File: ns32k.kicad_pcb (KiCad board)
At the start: 4 copper layers, 145.5 x 89.6 mm, 141 parts, among them J1 +5V SUPPLY, J2 3V3 Serial, J3 USB_C_USB2.0_16P, J4 RJ45, SW1 RESET, SW2 SW_DIP_x04, U1 NS32201, U10 74AHC373, U11 74AHC373, U12 74AHC138, U13 AS6C6416-55, U14 MT29F8G08ABACA, U15 MX29LV040C, U16 MX29LV040C, U17 ST16C550, U18 CP2102N, U19 74AHC32, U2 LM3671, U20 74AHC1GU04, U21 KSZ8851-16MLL, U22 74AHC245, U3 NS32016, U4 NS32082, U5 NS32202, U6 74AHC08, U7 74AHC245, U8 74AHC245, U9 74AHC373, Y1 12.00000MHz, Y2 7.3728MHz, Y3 25MHz

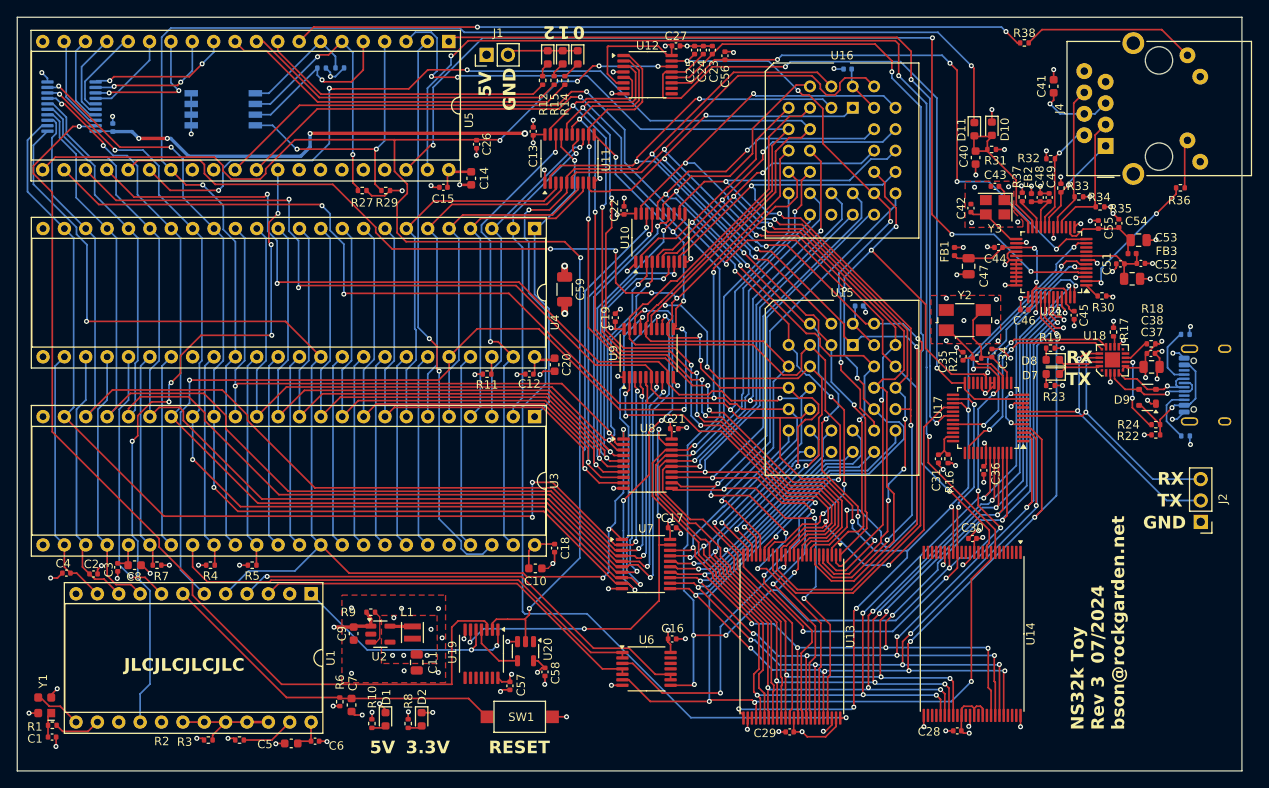
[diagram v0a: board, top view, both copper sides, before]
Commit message: Rework RESET/RST: see Changelist
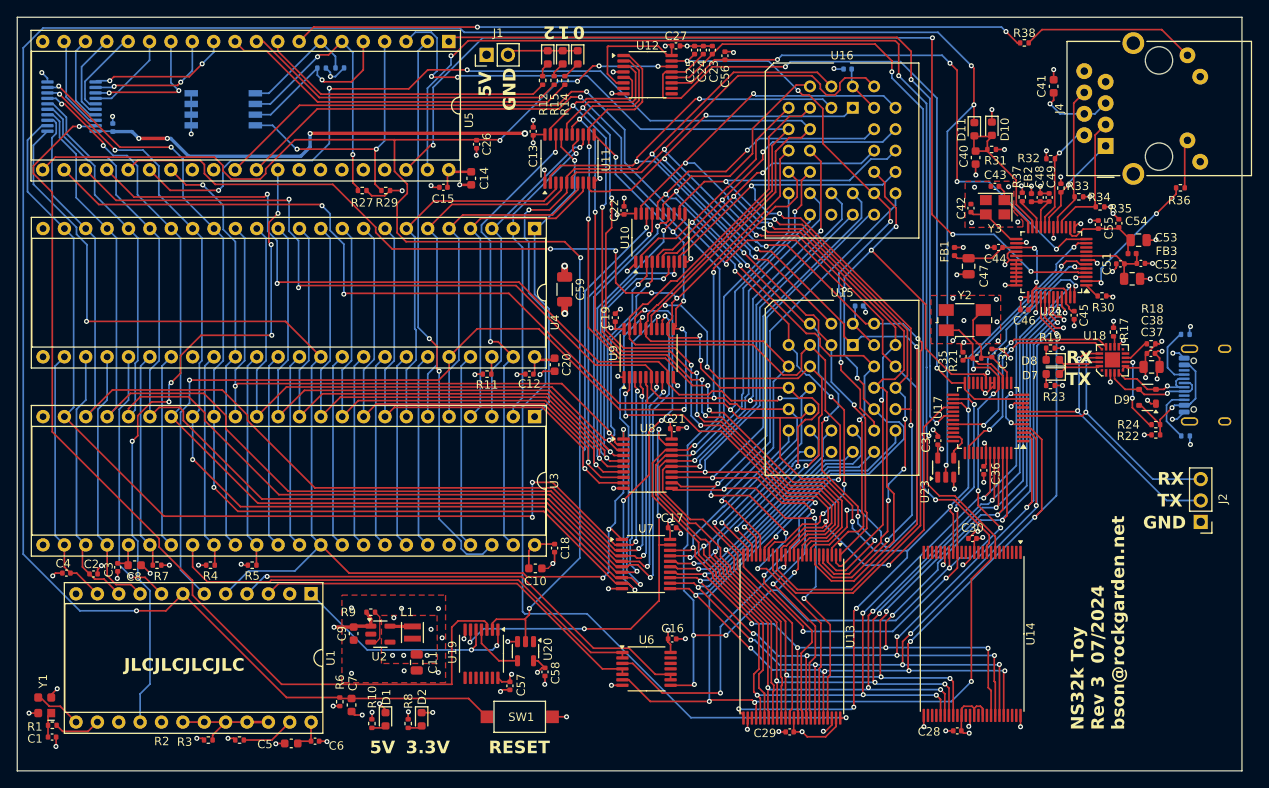
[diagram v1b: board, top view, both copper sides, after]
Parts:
- removed R16: 47k, Resistor_SMD:R_0402_1005Metric
- added U23: 74AHC1GU04, Package_TO_SOT_SMD:SOT-23-5, F.Cu at (169.2, 103.7)
- moved C31 2.15 mm to (168.2, 100.5)
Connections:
- C31 pad 2: Net-(U17A-RESET) -> GND
- C7 pad 1: Net-(U1B-~{RSTI}) -> /Ethernet/~{RESET}
- R6 pad 2: Net-(U1B-~{RSTI}) -> /Ethernet/~{RESET}
- SW1 pad 1: Net-(U1B-~{RSTI}) -> /Ethernet/~{RESET}
- U1 pad 7: Net-(U1B-~{RSTI}) -> /Ethernet/~{RESET}
- U3 pad 34: /Ethernet/~{RESET} -> Net-(U3A-~{RST}/ABT)
- U4 pad 34: /Ethernet/~{RESET} -> Net-(U3A-~{RST}/ABT)
- U5 pad 27: /Ethernet/~{RESET} -> Net-(U3A-~{RST}/ABT)
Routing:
- net /Ethernet/~{RESET}: track 171.2 -> 292.6 mm, vias 2 -> 4
- net Net-(U3A-~{RST}/ABT): track 0.00 -> 49.8 mm, vias 0 -> 1
- net Net-(U1B-~{RSTI}): track 42.0 -> 0.00 mm
- net GND: track 143.8 -> 145.1 mm, vias 115 -> 116
- net /1GB x 8 NAND Flash/R/~{B}: track 134.1 -> 135.2 mm
- net /~{NAND}: track 92.2 -> 93.2 mm
- net Net-(U17B-XTAL2): track 11.0 -> 11.7 mm
- net +3V3: track 151.9 -> 152.5 mm

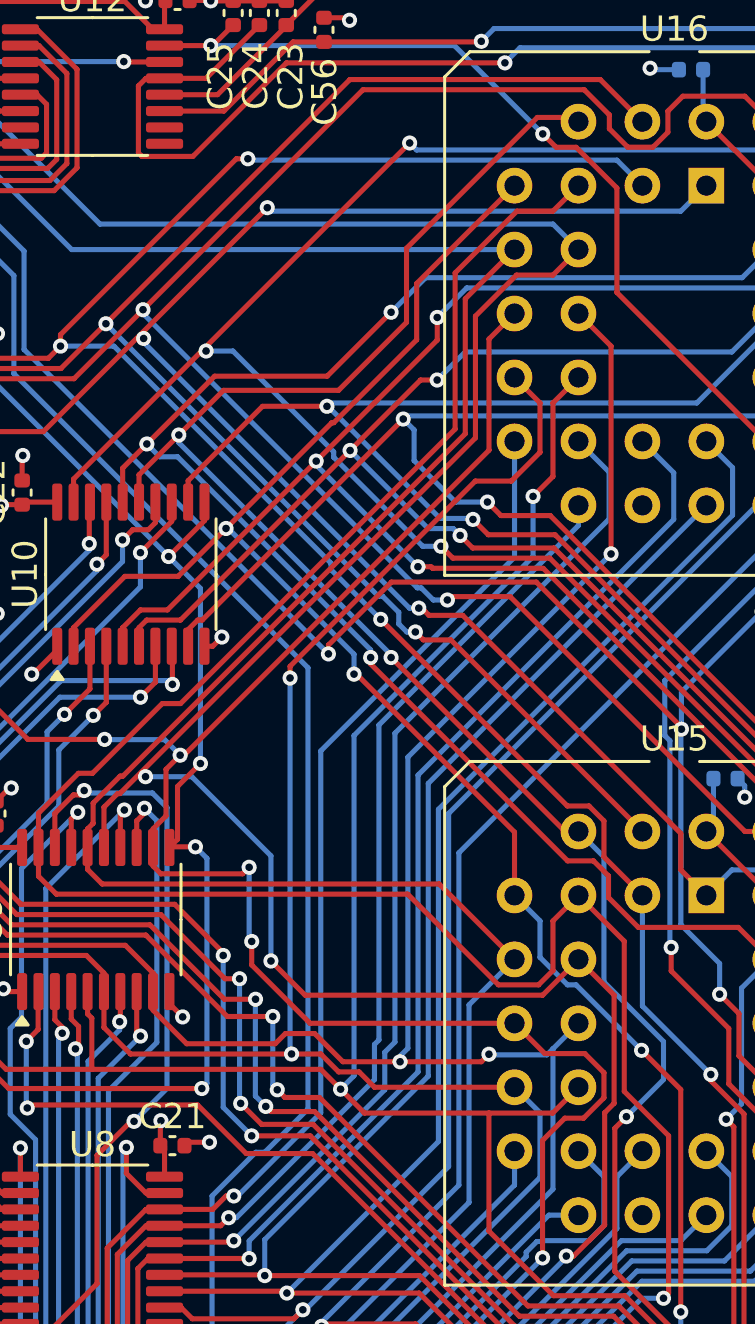
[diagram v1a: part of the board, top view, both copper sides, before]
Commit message: mark even/odd ROM banks
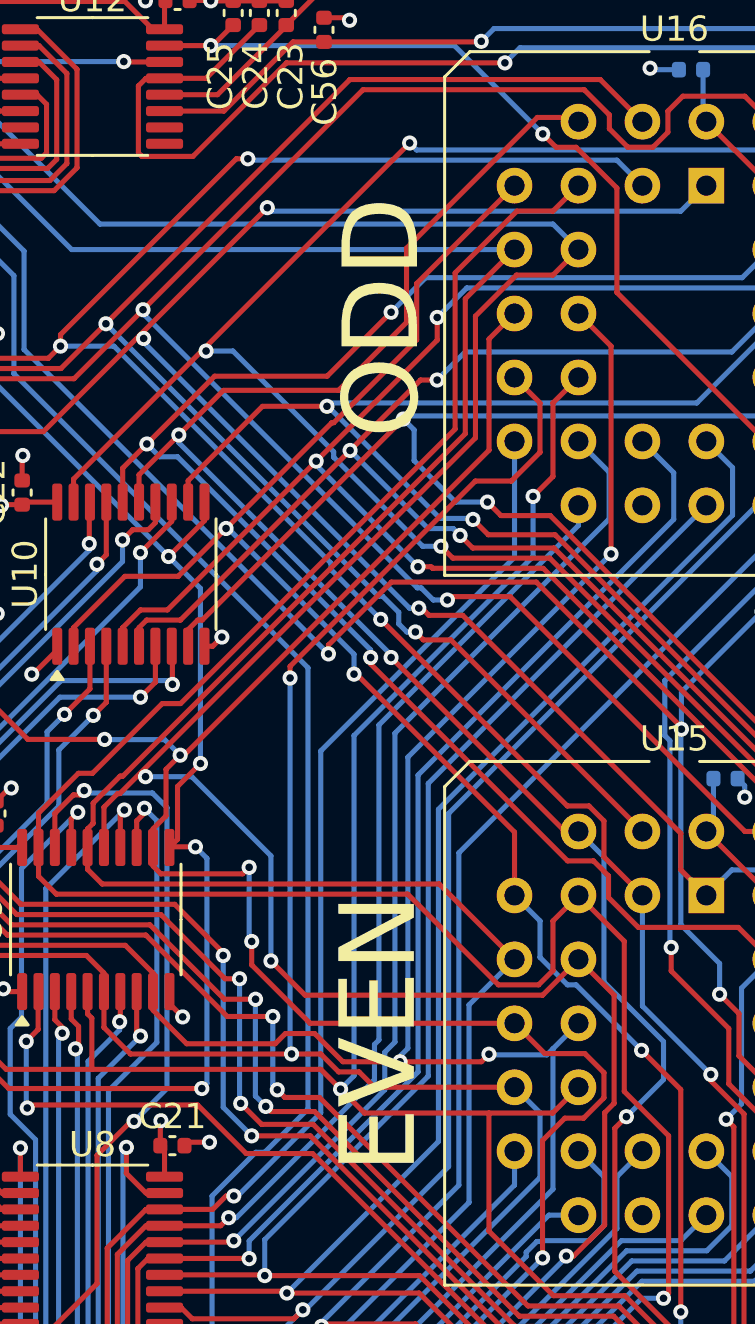
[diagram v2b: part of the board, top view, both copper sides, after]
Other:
- board text added: "EVEN"
- board text added: "ODD"
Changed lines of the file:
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@@
+		)
+	)
+	(gr_text "EVEN"
+		(at 146.8628 100.197029 90)
+		(layer "F.SilkS")
+		(effects
+			(font
+				(size 3 3)
+				(thickness 0.45)
+			)
+			(justify left bottom)
 		)
 	)
@@
 		)
 	)
+	(gr_text "ODD"
+		(at 143.2523 71.003029 -90)
+		(layer "F.SilkS")
+		(effects
+			(font
+				(size 3 3)
+				(thickness 0.45)
+			)
+			(justify left bottom mirror)
+		)
+	)

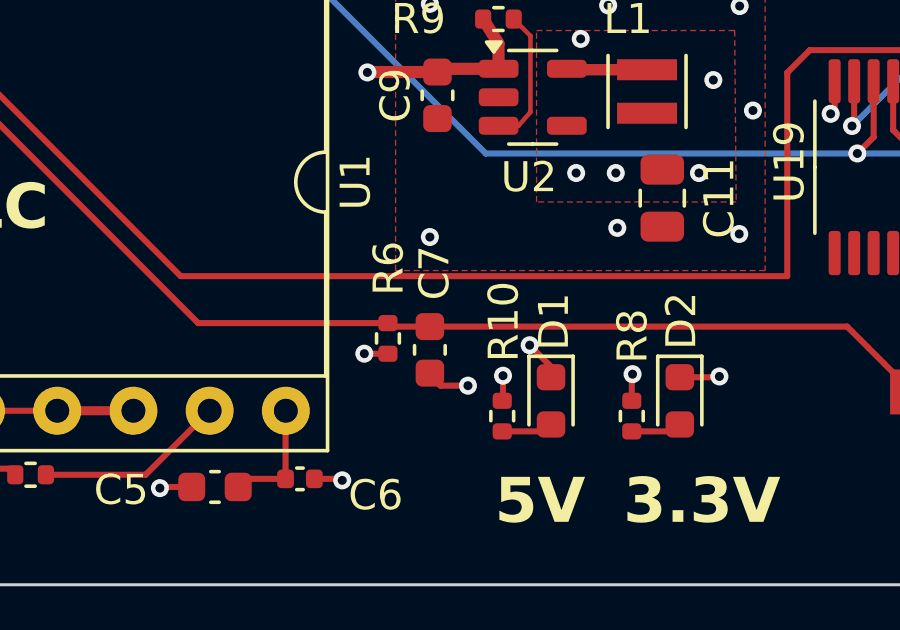
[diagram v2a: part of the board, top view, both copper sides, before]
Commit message: fix reset timing, should be 100us, not 100ms...
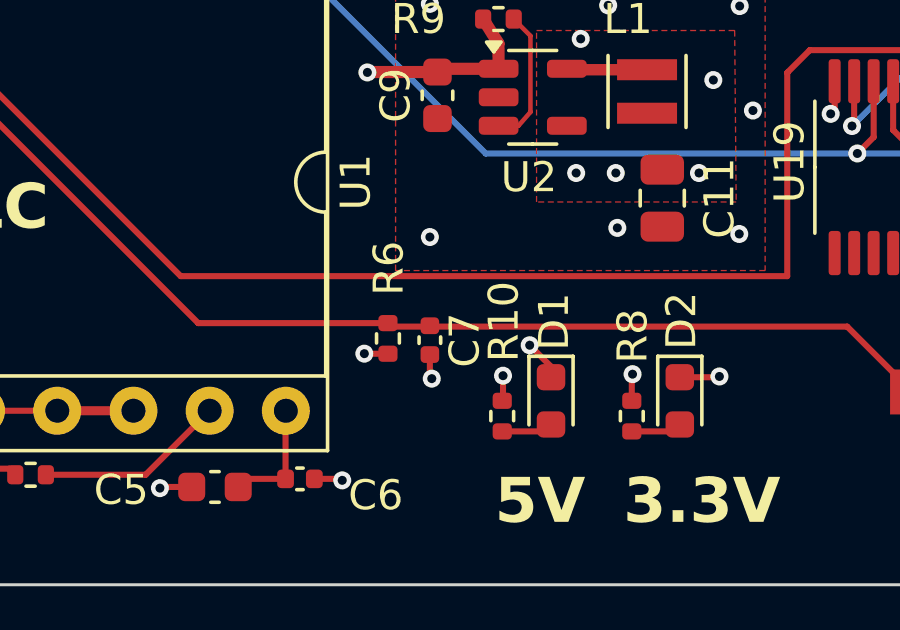
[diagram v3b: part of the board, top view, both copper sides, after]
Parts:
- C7: value 2.2µF -> 0.1µF; footprint Capacitor_SMD:C_0603_1608Metric -> Capacitor_SMD:C_0402_1005Metric
- R6: value 47k -> 1k
- moved C7 0.32 mm to (98.6, 131.6)
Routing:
- net GND: track 145.1 -> 144.4 mm
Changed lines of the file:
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@@
 			)
 		)
-		(property "Value" "47k"
+		(property "Value" "1k"
 			(at 0 1.17 90)
 			(layer "F.Fab")
@@
 		)
 	)
-	(footprint "Capacitor_SMD:C_0603_1608Metric"
+	(footprint "Capacitor_SMD:C_0402_1005Metric"
 		(layer "F.Cu")
-		(at 98.552 131.9462 -90)
-		(descr "Capacitor SMD 0603 (1608 Metric), square (rectangular) end terminal, IPC_7351 nominal, (Body size source: IPC-SM-782 page 76, https://www.pcb-3d.com/wordpress/wp-content/uploads/ipc-sm-782a_amendment_1_and_2.pdf), generated with kicad-footprint-generator")
+		(at 98.552 131.6228 -90)
+		(descr "Capacitor SMD 0402 (1005 Metric), square (rectangular) end terminal, IPC_7351 nominal, (Body size source: IPC-SM-782 page 76, https://www.pcb-3d.com/wordpress/wp-content/uploads/ipc-sm-782a_amendment_1_and_2.pdf), generated with kicad-footprint-generator")
 		(tags "capacitor")
 		(property "Reference" "C7"
-			(at -2.5674 -0.1524 90)
+			(at 0 -1.16 -90)
 			(layer "F.SilkS")
 			(effects
@@
 			)
 		)
-		(property "Value" "2.2µF"
-			(at 0 1.43 90)
+		(property "Value" "0.1µF"
+			(at 0 1.16 -90)
 			(layer "F.Fab")
 			(effects
@@
 			)
 		)
-		(property "Footprint" "Capacitor_SMD:C_0603_1608Metric"
+		(property "Footprint" "Capacitor_SMD:C_0402_1005Metric"
 			(at 0 0 -90)
 			(unlocked yes)
@@
 		(attr smd)
 		(fp_line
-			(start -0.14058 0.51)
-			(end 0.14058 0.51)
+			(start -0.107836 0.36)
+			(end 0.107836 0.36)
 			(stroke
 				(width 0.12)
@@
 		)
 		(fp_line
-			(start -0.14058 -0.51)
-			(end 0.14058 -0.51)
+			(start -0.107836 -0.36)
+			(end 0.107836 -0.36)
 			(stroke
 				(width 0.12)
@@
 		)
 		(fp_line
-			(start -1.48 0.73)
-			(end -1.48 -0.73)
+			(start -0.91 0.46)
+			(end -0.91 -0.46)
 			(stroke
 				(width 0.05)
@@
 		)
 		(fp_line
-			(start 1.48 0.73)
-			(end -1.48 0.73)
+			(start 0.91 0.46)
+			(end -0.91 0.46)
 			(stroke
 				(width 0.05)
@@
 		)
 		(fp_line
-			(start -1.48 -0.73)
-			(end 1.48 -0.73)
+			(start -0.91 -0.46)
+			(end 0.91 -0.46)
 			(stroke
 				(width 0.05)
@@
 		)
 		(fp_line
-			(start 1.48 -0.73)
-			(end 1.48 0.73)
+			(start 0.91 -0.46)
+			(end 0.91 0.46)
 			(stroke
 				(width 0.05)
@@
 		)
 		(fp_line
-			(start -0.8 0.4)
-			(end -0.8 -0.4)
+			(start -0.5 0.25)
+			(end -0.5 -0.25)
 			(stroke
 				(width 0.1)
@@
 		)
 		(fp_line
-			(start 0.8 0.4)
-			(end -0.8 0.4)
+			(start 0.5 0.25)
+			(end -0.5 0.25)
 			(stroke
 				(width 0.1)
@@
 		)
 		(fp_line
-			(start -0.8 -0.4)
-			(end 0.8 -0.4)
+			(start -0.5 -0.25)
+			(end 0.5 -0.25)
 			(stroke
 				(width 0.1)
@@
 		)
 		(fp_line
-			(start 0.8 -0.4)
-			(end 0.8 0.4)
+			(start 0.5 -0.25)
+			(end 0.5 0.25)
 			(stroke
 				(width 0.1)
@@
 		)
 		(fp_text user "${REFERENCE}"
-			(at 0 0 90)
+			(at 0 0 -90)
 			(layer "F.Fab")
 			(effects
 				(font
-					(size 0.4 0.4)
-					(thickness 0.06)
+					(size 0.25 0.25)
+					(thickness 0.04)
 				)
 			)
 		)
 		(pad "1" smd roundrect
-			(at -0.775 0 270)
-			(size 0.9 0.95)
+			(at -0.48 0 270)
+			(size 0.56 0.62)
 			(layers "F.Cu" "F.Paste" "F.Mask")
 			(roundrect_rratio 0.25)
@@
 		)
 		(pad "2" smd roundrect
-			(at 0.775 0 270)
-			(size 0.9 0.95)
+			(at 0.48 0 270)
+			(size 0.56 0.62)
 			(layers "F.Cu" "F.Paste" "F.Mask")
 			(roundrect_rratio 0.25)
@@
 			(pintype "passive")
 		)
-		(model "${KICAD8_3DMODEL_DIR}/Capacitor_SMD.3dshapes/C_0603_1608Metric.wrl"
+		(model "${KICAD8_3DMODEL_DIR}/Capacitor_SMD.3dshapes/C_0402_1005Metric.wrl"
 			(offset
 				(xyz 0 0 0)
@@
 	)
 	(segment
-		(start 98.9076 133.14)
-		(end 99.822 133.14)
-		(width 0.2032)
-		(layer "F.Cu")
-		(net 1)
-	)
-	(segment
 		(start 194.5762 90.7142)
 		(end 194.03 90.168)
@@
 	)
 	(segment
+		(start 98.552 132.1028)
+		(end 98.552 132.842)
+		(width 0.2032)
+		(layer "F.Cu")
+		(net 1)
+	)
+	(segment
 		(start 138.870375 78.909)
 		(end 138.506775 79.2726)
@@
 	)
 	(segment
-		(start 98.5012 132.7336)
-		(end 98.9076 133.14)
-		(width 0.2032)
-		(layer "F.Cu")
-		(net 1)
-	)
-	(segment
 		(start 113.411 66.5988)
 		(end 113.3856 66.6242)
@@
 	)
 	(segment
+		(start 98.552 132.842)
+		(end 98.6155 132.9055)
+		(width 0.2032)
+		(layer "F.Cu")
+		(net 1)
+	)
+	(segment
 		(start 130.683 118.1196)
 		(end 129.0898 118.1196)
@@
 	)
 	(via
-		(at 99.822 133.14)
+		(at 98.6155 132.9055)
 		(size 0.6)
 		(drill 0.3)

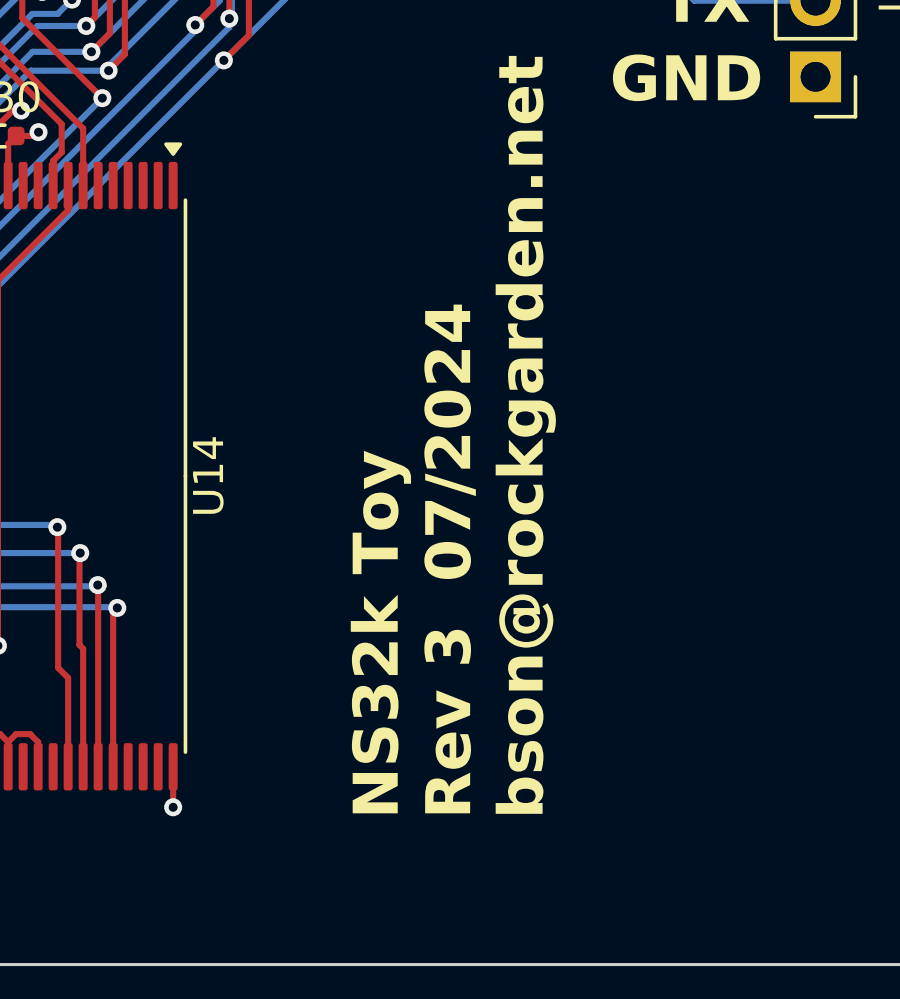
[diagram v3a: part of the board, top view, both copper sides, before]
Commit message: update text to say rev 4
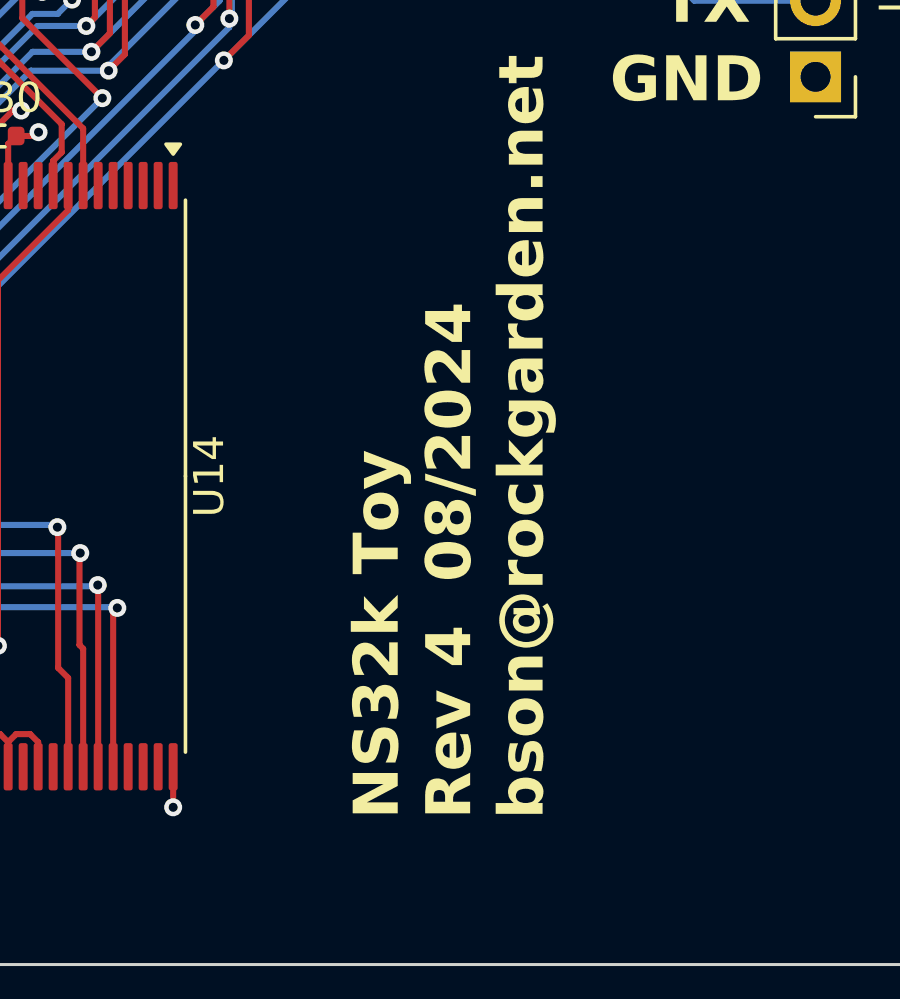
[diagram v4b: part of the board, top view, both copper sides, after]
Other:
- board text added: "NS32k Toy Rev 4 08/2024 bson@rockgarden.net"
- board text removed: "NS32k Toy Rev 3 07/2024 bson@rockgarden.net"
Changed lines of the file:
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@@
 	(paper "USLetter")
 	(title_block
-		(date "2024-07-30")
-		(rev "3")
+		(date "2024-08-01")
+		(rev "4")
 	)
 	(layers
@@
 		)
 	)
-	(gr_text "NS32k Toy\nRev 3  07/2024\nbson@rockgarden.net"
+	(gr_text "NS32k Toy\nRev 4  08/2024\nbson@rockgarden.net"
 		(at 190.5508 134.9248 90)
 		(layer "F.SilkS")
